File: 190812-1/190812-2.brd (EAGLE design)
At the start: 45 x 29 mm, 18 parts, among them U22 ESPRUINO_PICO_SMDONLY, U6 MCP6071T-E/OT

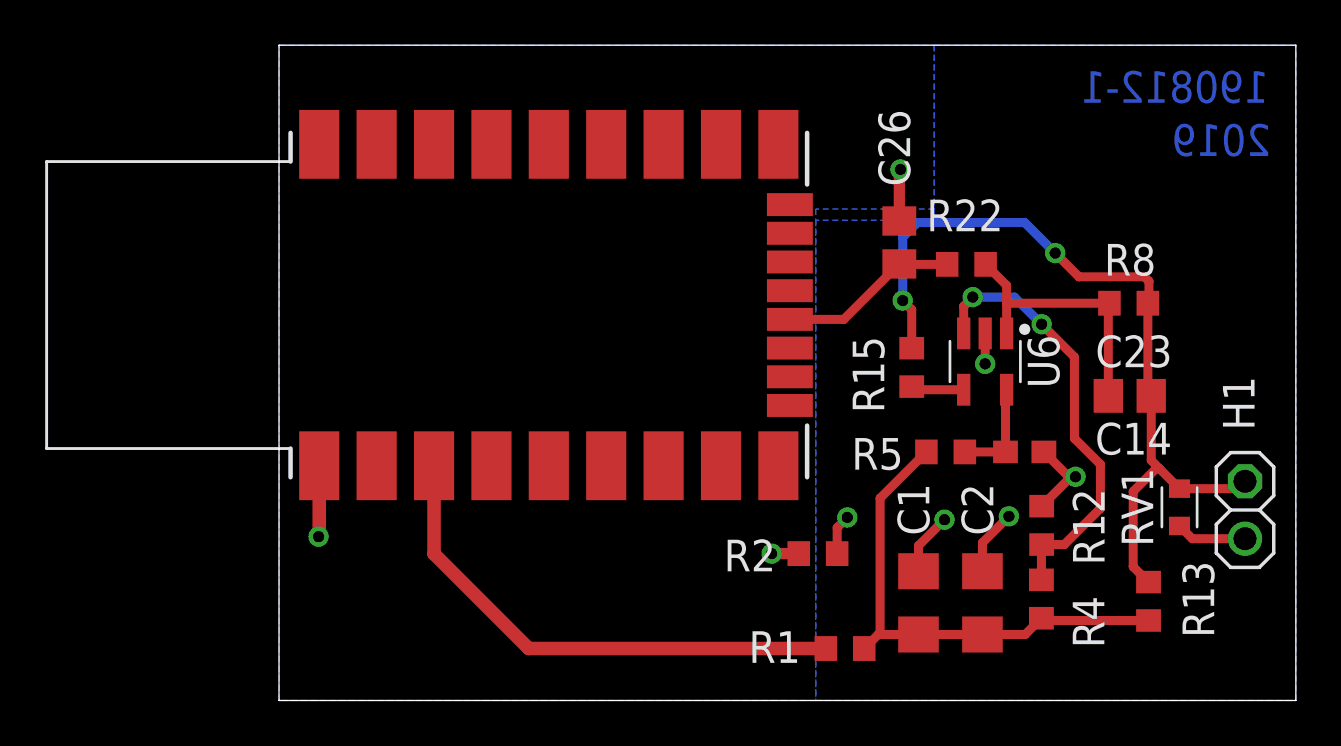
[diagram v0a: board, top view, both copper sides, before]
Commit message: Boards were ordered from the commit.  Sunstone circuits.
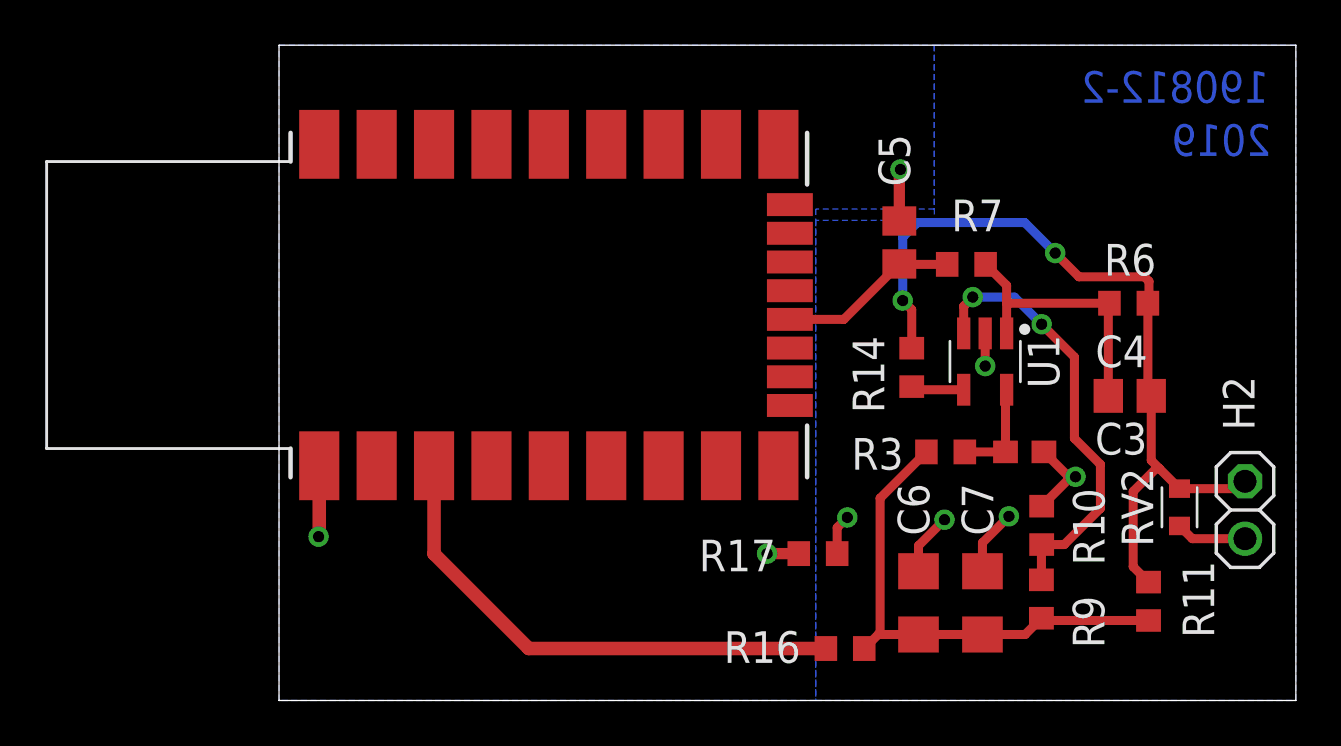
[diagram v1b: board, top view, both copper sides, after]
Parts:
- renumbered C1 to C6, C14 to C3, C2 to C7, C23 to C4, C26 to C5, H1 to H2, R1 to R16, R12 to R10, R13 to R11, R15 to R14, R2 to R17, R22 to R7, R4 to R9, R5 to R3, R8 to R6, RV1 to RV2, U22 to U2, U6 to U1
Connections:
- net +3V3 renamed +3V1
- net +3V3A renamed +3V3A1
- net FSR_OUT1 renamed FSR_OUT2
- net GND renamed GND1
- net GNDA renamed GNDA1
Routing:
- removed copper zone on layer 3, net +3V1
- removed copper zone on layer 2, net GND1
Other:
- board text added: "190812-2"
- board text removed: "190812-1"

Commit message: Fixed schematic corruption.  Reran CAM.
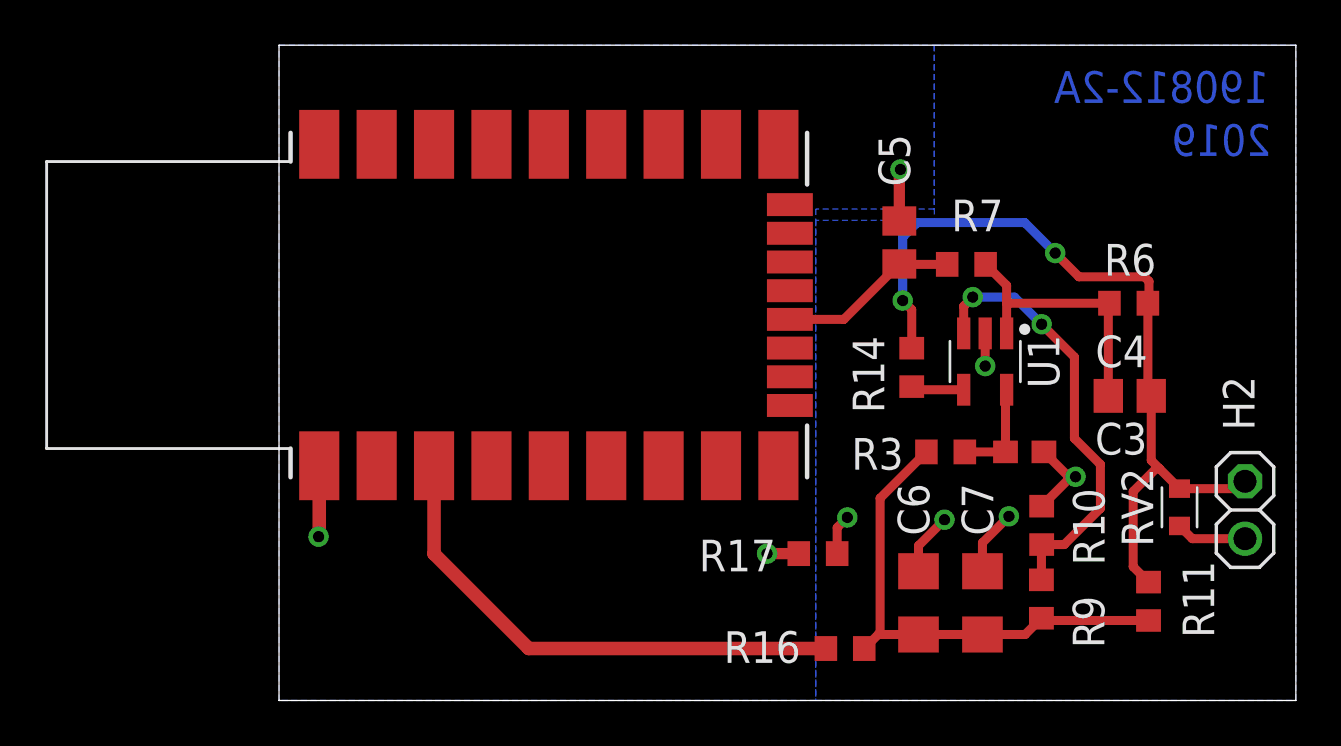
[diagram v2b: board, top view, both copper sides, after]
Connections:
- net +3V1 renamed +3V3
- net +3V3A1 renamed +3V3A
- net GND1 renamed GND
- new net GNDA: C3.2, C6.2, C7.2, H2.2, R10.1, R17.1, RV2.1
- net GNDA1: no longer C3.2, C6.2, C7.2, H2.2, R10.1, R17.1, RV2.1
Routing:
- net GNDA1: track 15.9 -> 1.45 mm, vias 5 -> 1
- net GNDA: track 0.00 -> 14.5 mm, vias 0 -> 4
- added copper zone on layer 16, net GNDA
- removed copper zone on layer 16, net GNDA1
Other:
- board text added: "190812-2A"
- board text removed: "190812-2"
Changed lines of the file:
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@@
 <wire x1="45" y1="29" x2="0" y2="29" width="0" layer="20"/>
 <wire x1="0" y1="29" x2="0" y2="0" width="0" layer="20"/>
-<text x="43.8" y="26.45" size="1.4" layer="16" ratio="18" rot="MR0">190812-2</text>
+<text x="43.8" y="26.45" size="1.4" layer="16" ratio="18" rot="MR0">190812-2A</text>
 <text x="43.9" y="24.1" size="1.4" layer="16" ratio="18" rot="MR0">2019</text>
 </plain>
@@
 </elements>
 <signals>
-<signal name="GND1">
-<contactref element="C5" pad="2"/>
-<contactref element="U2" pad="GND"/>
-<contactref element="R17" pad="2"/>
-<polygon width="0.1524" layer="16" isolate="0.5">
-<vertex x="0" y="0"/>
-<vertex x="0" y="29"/>
-<vertex x="29" y="29"/>
-<vertex x="29" y="21.75"/>
-<vertex x="23.75" y="21.75"/>
-<vertex x="23.75" y="0"/>
-</polygon>
-<wire x1="1.78" y1="10.388" x2="1.78" y2="7.28" width="0.6" layer="1"/>
-<wire x1="1.78" y1="7.28" x2="1.75" y2="7.25" width="0.6" layer="1"/>
-<via x="1.75" y="7.25" extent="1-16" drill="0.5"/>
-<wire x1="23" y1="6.5" x2="21.6" y2="6.5" width="0.5" layer="1"/>
-<via x="21.6" y="6.5" extent="1-16" drill="0.5"/>
-<wire x1="27.45" y1="21.22" x2="27.45" y2="23.45" width="0.5" layer="1"/>
-<wire x1="27.45" y1="23.45" x2="27.5" y2="23.5" width="0.5" layer="1"/>
-<via x="27.5" y="23.5" extent="1-16" drill="0.5"/>
-</signal>
-<signal name="+3V1">
-<contactref element="U2" pad="3.3V"/>
-<contactref element="R16" pad="1"/>
-<wire x1="6.86" y1="10.388" x2="6.86" y2="6.49" width="0.6" layer="1"/>
-<wire x1="11.05" y1="2.3" x2="24.2" y2="2.3" width="0.6" layer="1"/>
-<wire x1="6.86" y1="6.49" x2="11.05" y2="2.3" width="0.6" layer="1"/>
-</signal>
 <signal name="N$1">
 <contactref element="R3" pad="1"/>
@@
 </signal>
 <signal name="GNDA1">
-<contactref element="R10" pad="1"/>
-<contactref element="RV2" pad="1"/>
-<contactref element="C7" pad="2"/>
-<contactref element="C6" pad="2"/>
-<contactref element="H2" pad="2"/>
-<contactref element="C3" pad="2"/>
 <contactref element="U1" pad="2"/>
-<contactref element="R17" pad="1"/>
-<polygon width="0.25" layer="16" isolate="0.5" rank="2">
-<vertex x="45" y="29"/>
-<vertex x="29" y="29"/>
-<vertex x="29" y="21.25"/>
-<vertex x="23.75" y="21.25"/>
-<vertex x="23.75" y="0"/>
-<vertex x="45" y="0"/>
-</polygon>
-<wire x1="24.7" y1="7.65" x2="24.7" y2="6.5" width="0.4" layer="1"/>
-<wire x1="24.7" y1="7.65" x2="25.15" y2="8.1" width="0.4" layer="1"/>
-<via x="25.15" y="8.1" extent="1-16" drill="0.5"/>
-<wire x1="28.3" y1="5.72" x2="28.3" y2="6.85" width="0.4" layer="1"/>
-<wire x1="28.3" y1="6.85" x2="29.45" y2="8" width="0.4" layer="1"/>
-<via x="29.45" y="8" extent="1-16" drill="0.5"/>
-<wire x1="42.75" y1="7.16" x2="40.4154" y2="7.16" width="0.4" layer="1"/>
-<wire x1="40.4154" y1="7.16" x2="39.85" y2="7.7254" width="0.4" layer="1"/>
-<wire x1="35.05" y1="9.9" x2="33.75" y2="8.6" width="0.4" layer="1"/>
-<wire x1="35.05" y1="9.9" x2="35.25" y2="9.9" width="0.4" layer="1"/>
-<via x="35.25" y="9.9" extent="1-16" drill="0.5"/>
-<wire x1="33.85" y1="11" x2="34.95" y2="9.9" width="0.4" layer="1"/>
-<wire x1="34.95" y1="9.9" x2="35.25" y2="9.9" width="0.4" layer="1"/>
 <wire x1="31.25" y1="16.2472" x2="31.25" y2="14.8" width="0.4" layer="1"/>
 <via x="31.25" y="14.8" extent="1-16" drill="0.5"/>
-<wire x1="31.13" y1="5.72" x2="31.13" y2="6.98" width="0.4" layer="1"/>
-<wire x1="31.13" y1="6.98" x2="32.3" y2="8.15" width="0.4" layer="1"/>
-<via x="32.3" y="8.15" extent="1-16" drill="0.5"/>
-</signal>
-<signal name="+3V3A1">
-<contactref element="R3" pad="2"/>
-<contactref element="R9" pad="2"/>
-<contactref element="R11" pad="2"/>
-<contactref element="R16" pad="2"/>
-<contactref element="C6" pad="1"/>
-<contactref element="C7" pad="1"/>
-<wire x1="38.48" y1="3.54" x2="33.84" y2="3.54" width="0.4" layer="1"/>
-<wire x1="33.84" y1="3.54" x2="33.74" y2="3.64" width="0.4" layer="1"/>
-<wire x1="31.13" y1="2.92" x2="28.3" y2="2.92" width="0.4" layer="1"/>
-<wire x1="33.74" y1="3.64" x2="33.02" y2="2.92" width="0.4" layer="1"/>
-<wire x1="33.02" y1="2.92" x2="31.13" y2="2.92" width="0.4" layer="1"/>
-<wire x1="25.9" y1="2.3" x2="26.52" y2="2.92" width="0.4" layer="1"/>
-<wire x1="26.52" y1="2.92" x2="28.3" y2="2.92" width="0.4" layer="1"/>
-<wire x1="26.52" y1="2.92" x2="26.6" y2="3" width="0.4" layer="1"/>
-<wire x1="26.6" y1="8.95" x2="28.65" y2="11" width="0.4" layer="1"/>
-<wire x1="26.6" y1="3" x2="26.6" y2="8.95" width="0.4" layer="1"/>
 </signal>
 <signal name="VREF">
@@
 <wire x1="28.1372" y1="13.7528" x2="28" y2="13.89" width="0.4" layer="1"/>
 </signal>
+<signal name="GND">
+<contactref element="U2" pad="GND"/>
+<wire x1="1.78" y1="10.388" x2="1.78" y2="7.28" width="0.6" layer="1"/>
+<wire x1="1.78" y1="7.28" x2="1.75" y2="7.25" width="0.6" layer="1"/>
+<via x="1.75" y="7.25" extent="1-16" drill="0.5"/>
+<contactref element="R17" pad="2"/>
+<wire x1="23" y1="6.5" x2="21.6" y2="6.5" width="0.5" layer="1"/>
+<via x="21.6" y="6.5" extent="1-16" drill="0.5"/>
+<contactref element="C5" pad="2"/>
+<wire x1="27.45" y1="21.22" x2="27.45" y2="23.45" width="0.5" layer="1"/>
+<wire x1="27.45" y1="23.45" x2="27.5" y2="23.5" width="0.5" layer="1"/>
+<via x="27.5" y="23.5" extent="1-16" drill="0.5"/>
+<polygon width="0.1524" layer="16" isolate="0.5">
+<vertex x="0" y="0"/>
+<vertex x="0" y="29"/>
+<vertex x="29" y="29"/>
+<vertex x="29" y="21.75"/>
+<vertex x="23.75" y="21.75"/>
+<vertex x="23.75" y="0"/>
+</polygon>
+</signal>
+<signal name="+3V3">
+<contactref element="U2" pad="3.3V"/>
+<contactref element="R16" pad="1"/>
+<wire x1="6.86" y1="10.388" x2="6.86" y2="6.49" width="0.6" layer="1"/>
+<wire x1="11.05" y1="2.3" x2="24.2" y2="2.3" width="0.6" layer="1"/>
+<wire x1="6.86" y1="6.49" x2="11.05" y2="2.3" width="0.6" layer="1"/>
+</signal>
+<signal name="+3V3A">
+<contactref element="R16" pad="2"/>
+<contactref element="C6" pad="1"/>
+<contactref element="C7" pad="1"/>
+<wire x1="31.13" y1="2.92" x2="28.3" y2="2.92" width="0.4" layer="1"/>
+<contactref element="R11" pad="2"/>
+<contactref element="R9" pad="2"/>
+<wire x1="33.84" y1="3.54" x2="33.74" y2="3.64" width="0.4" layer="1"/>
+<wire x1="33.74" y1="3.64" x2="33.02" y2="2.92" width="0.4" layer="1"/>
+<contactref element="R3" pad="2"/>
+<wire x1="26.52" y1="2.92" x2="26.6" y2="3" width="0.4" layer="1"/>
+<wire x1="26.6" y1="8.95" x2="28.65" y2="11" width="0.4" layer="1"/>
+<wire x1="26.6" y1="3" x2="26.6" y2="8.95" width="0.4" layer="1"/>
+<wire x1="33.02" y1="2.92" x2="31.13" y2="2.92" width="0.4" layer="1"/>
+<wire x1="28.3" y1="2.92" x2="26.52" y2="2.92" width="0.4" layer="1"/>
+<wire x1="25.9" y1="2.3" x2="26.52" y2="2.92" width="0.4" layer="1"/>
+<wire x1="38.48" y1="3.54" x2="33.84" y2="3.54" width="0.4" layer="1"/>
+</signal>
+<signal name="GNDA">
+<contactref element="C7" pad="2"/>
+<contactref element="C6" pad="2"/>
+<contactref element="R17" pad="1"/>
+<wire x1="24.7" y1="7.65" x2="24.7" y2="6.5" width="0.4" layer="1"/>
+<wire x1="24.7" y1="7.65" x2="25.15" y2="8.1" width="0.4" layer="1"/>
+<via x="25.15" y="8.1" extent="1-16" drill="0.5"/>
+<wire x1="28.3" y1="5.72" x2="28.3" y2="6.85" width="0.4" layer="1"/>
+<wire x1="28.3" y1="6.85" x2="29.45" y2="8" width="0.4" layer="1"/>
+<via x="29.45" y="8" extent="1-16" drill="0.5"/>
+<wire x1="31.13" y1="5.72" x2="31.13" y2="6.98" width="0.4" layer="1"/>
+<wire x1="31.13" y1="6.98" x2="32.3" y2="8.15" width="0.4" layer="1"/>
+<via x="32.3" y="8.15" extent="1-16" drill="0.5"/>
+<contactref element="H2" pad="2"/>
+<contactref element="RV2" pad="1"/>
+<wire x1="39.85" y1="7.7254" x2="40.4154" y2="7.16" width="0.4" layer="1"/>
+<contactref element="C3" pad="2"/>
+<contactref element="R10" pad="1"/>
+<wire x1="35.05" y1="9.9" x2="33.75" y2="8.6" width="0.4" layer="1"/>
+<wire x1="35.05" y1="9.9" x2="35.25" y2="9.9" width="0.4" layer="1"/>
+<via x="35.25" y="9.9" extent="1-16" drill="0.5"/>
+<wire x1="34.95" y1="9.9" x2="35.25" y2="9.9" width="0.4" layer="1"/>
+<polygon width="0.25" layer="16" isolate="0.5" rank="2">
+<vertex x="45" y="29"/>
+<vertex x="29" y="29"/>
+<vertex x="29" y="21.25"/>
+<vertex x="23.75" y="21.25"/>
+<vertex x="23.75" y="0"/>
+<vertex x="45" y="0"/>
+</polygon>
+<wire x1="40.4154" y1="7.16" x2="42.75" y2="7.16" width="0.4" layer="1"/>
+<wire x1="33.85" y1="11" x2="34.95" y2="9.9" width="0.4" layer="1"/>
+</signal>
 </signals>

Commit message: added espruino code.  WARNING eagle was corrupted double check.
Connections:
- removed net GNDA1: U1.2
- net GNDA: now also U1.2
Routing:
- net GNDA1: track 1.45 -> 0.00 mm, vias 1 -> 0
- net GNDA: track 14.5 -> 15.9 mm, vias 4 -> 5
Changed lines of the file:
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@@
 <wire x1="27.47" y1="19.3" x2="27.45" y2="19.32" width="0.4" layer="1"/>
-</signal>
-<signal name="GNDA1">
-<contactref element="U1" pad="2"/>
-<wire x1="31.25" y1="16.2472" x2="31.25" y2="14.8" width="0.4" layer="1"/>
-<via x="31.25" y="14.8" extent="1-16" drill="0.5"/>
 </signal>
 <signal name="VREF">
@@
 <wire x1="40.4154" y1="7.16" x2="42.75" y2="7.16" width="0.4" layer="1"/>
 <wire x1="33.85" y1="11" x2="34.95" y2="9.9" width="0.4" layer="1"/>
+<contactref element="U1" pad="2"/>
+<wire x1="31.25" y1="16.2472" x2="31.25" y2="14.8" width="0.4" layer="1"/>
+<via x="31.25" y="14.8" extent="1-16" drill="0.5"/>
+<wire x1="35.25" y1="9.9" x2="39.85" y2="7.7254" width="0" layer="19" extent="1-1"/>
+<wire x1="32.3" y1="8.15" x2="33.75" y2="8.6" width="0" layer="19" extent="1-1"/>
+<wire x1="29.45" y1="8" x2="31.13" y2="6.98" width="0" layer="19" extent="1-1"/>
+<wire x1="25.15" y1="8.1" x2="28.3" y2="6.85" width="0" layer="19" extent="1-1"/>
+<wire x1="31.25" y1="14.8" x2="33.85" y2="11" width="0" layer="19" extent="1-1"/>
 </signal>
 </signals>
